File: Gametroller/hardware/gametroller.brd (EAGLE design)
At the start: 45.7 x 31.8 mm, 49 parts, among them J1 microUSB, J2 PJ-002AH-SMT-TR, J3 USB-A, SW1 SPST_TACT-KMR2, U1 LP5907MFX-3.3/NOPB, U16 AOZ1280CI, U2 TPS2115AIPWRQ1-SON8, U4 ATSAMD21G18_QFN, X2 32.768

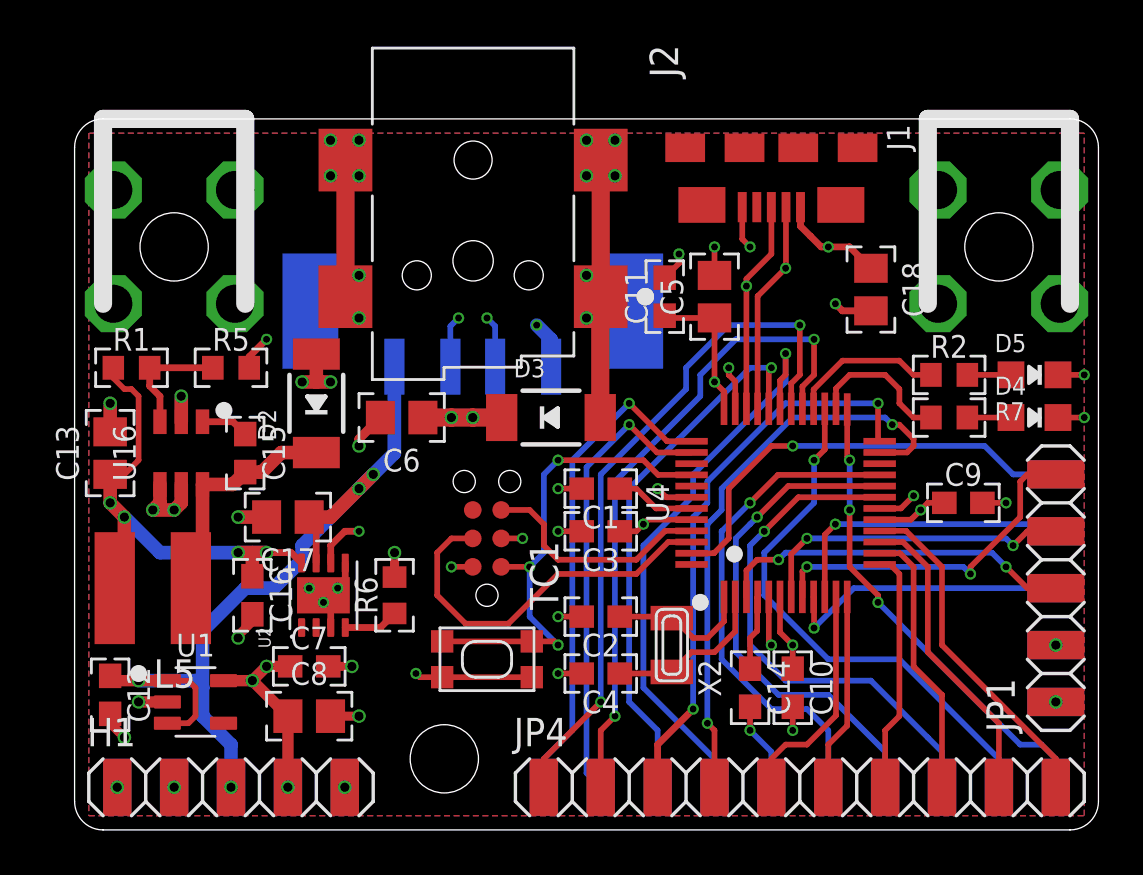
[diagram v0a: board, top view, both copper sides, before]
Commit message: Minor changes to PCB
* Added "power good" LED to 3V3 rail
* Removed silkscreen text for part numbers (just not enough room)
* Increased voltage output on 5V step-down converter
* Added silkscreen text for pin numbers
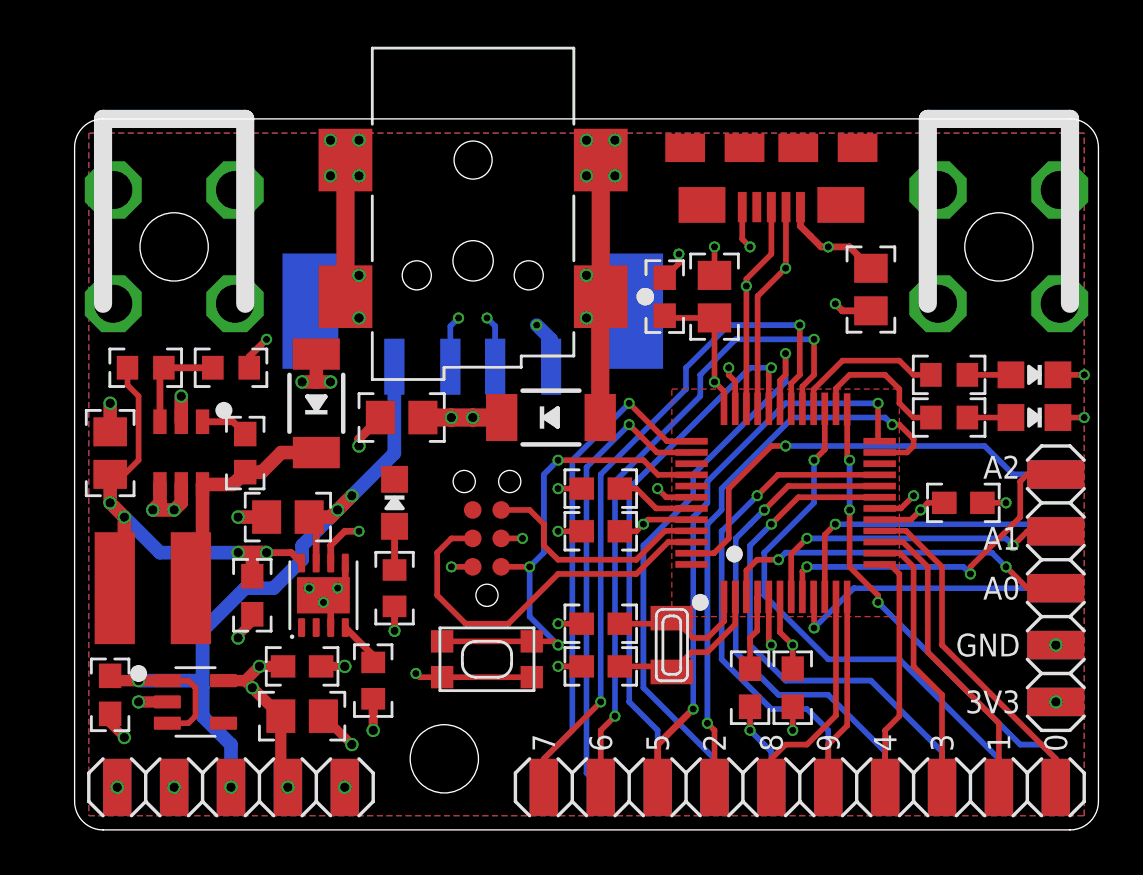
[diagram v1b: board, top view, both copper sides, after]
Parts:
- added D1: RED, gametroller:CHIPLED_0805_NOOUTLINE
- added R3: 1k, gametroller:R0603
- R1: value 51k -> 56k
- moved R6 3.93 mm to (13.3, 6.67), turned to 270 degrees
- moved R1 0.63 mm to (3.17, 20.6)
- moved C2 0.32 mm to (23.5, 9.21)
- moved C4 0.32 mm to (23.5, 7.30)
- moved C7 0.32 mm to (10.2, 7.30)
- moved C8 0.32 mm to (10.2, 5.08)
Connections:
- new net N$3: D1.A, R3.2
- net +3V3: now also R3.1
- net GND: now also D1.C
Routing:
- net +5V: track 40.0 -> 37.8 mm
- net N$3: track 0.00 -> 1.95 mm
- net +3V3: track 26.2 -> 27.1 mm, vias 9 -> 10
- net GND: track 61.5 -> 62.3 mm
- net N$11: track 5.42 -> 4.67 mm
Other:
- board text added: "0"
- board text added: "1"
- board text added: "10"
- board text added: "11"
- board text added: "2"
- board text added: "3"
- board text added: "3.3V - 48MHz"
- board text added: "3V3"
- board text added: "4"
- board text added: "5"
- board text added: "5V"
- board text added: "6"
- board text added: "7"
- board text added: "8"
- board text added: "9"
- board text added: "A0"
- board text added: "A1"
- board text added: "A2"
- board text added: "A3"
- board text added: "A4"
- board text added: "A5"
- board text added: "ATSAMD21G18"
- board text added: "FEATHER M0"
- board text added: "GAMETROLLER"
- board text added: "GND"
- board text added: "MISO"
- board text added: "MOSI"
- board text added: "RXD"
- board text added: "SCL"
- board text added: "SCLK"
- board text added: "SDA"
- board text added: "TXD"
- board text added: "VIN"
- board text removed: "ATSAMD21G18-48MHz"
